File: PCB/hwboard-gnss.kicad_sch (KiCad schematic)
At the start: 1 part, among them U1 TESEO-LIV3R

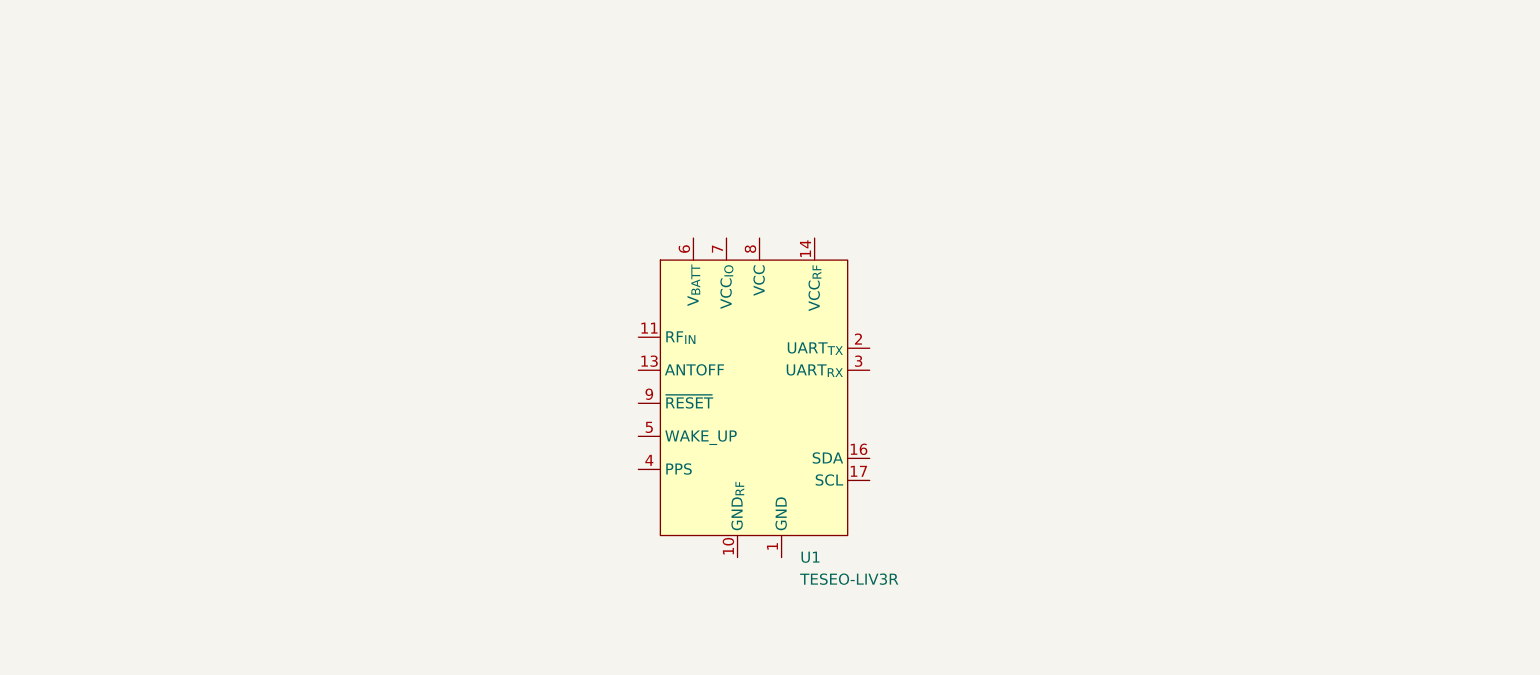
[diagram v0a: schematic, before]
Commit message: Update with gnss
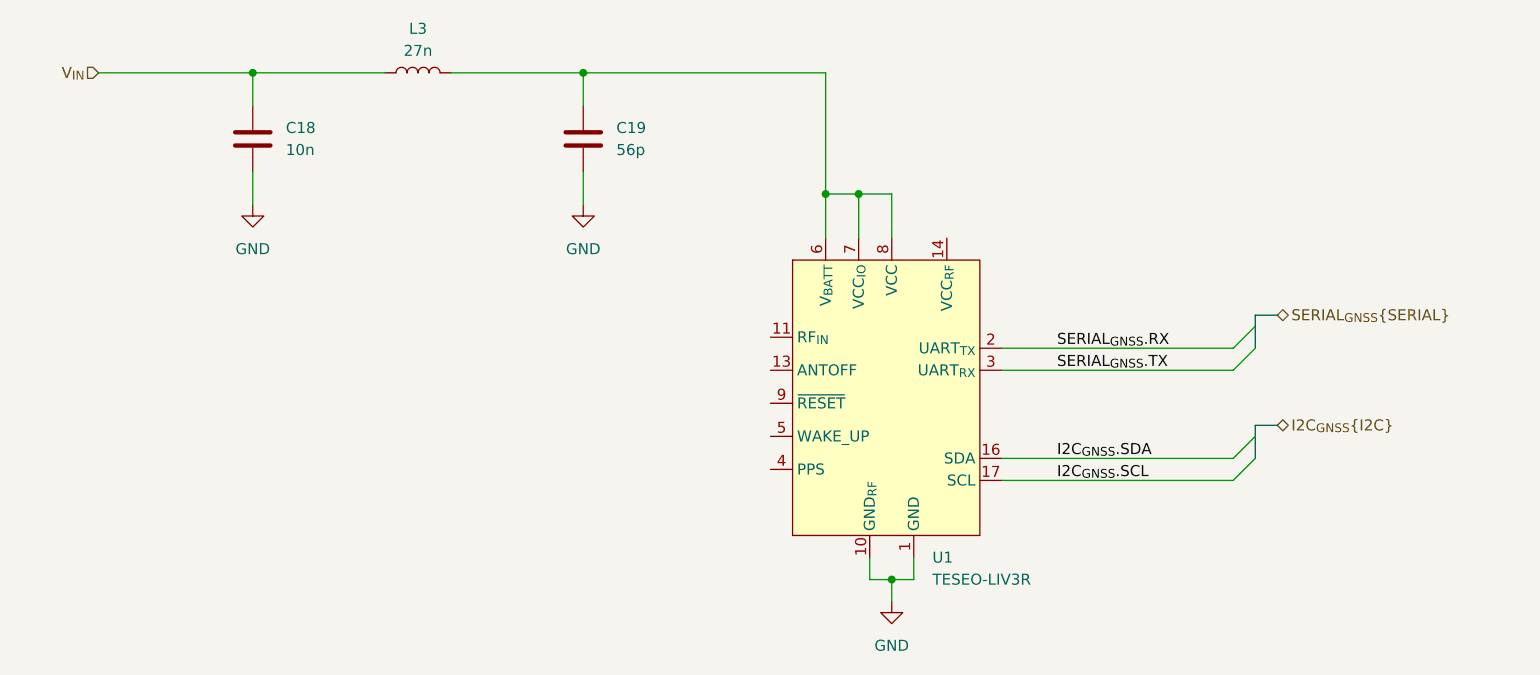
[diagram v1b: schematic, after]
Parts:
- added C18: 10n, symbol Device:C
- added C19: 56p, symbol Device:C
- added L3: 27n, symbol Device:L
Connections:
- net GND_{RF} is gone; now on net GND: U1.10 (GND_{RF}), U1.12 (GND_{RF})
- net GND: now reaches U1.1 (GND)
- net GND: now also C18.2, C19.2
- net I2C_{GNSS}.SDA: now reaches U1.16 (SDA)
- net I2C_{GNSS}.SCL: now reaches U1.17 (SCL)
- net SERIAL_{GNSS}.RX: now reaches U1.2 (UART_{TX})
- net SERIAL_{GNSS}.TX: now reaches U1.3 (UART_{RX})
- net at U1.6 (V_{BATT}): now also U1.7 (VCC_{IO}), U1.8 (VCC), C19.1, L3.2
- new net V_{IN}: C18.1, L3.1
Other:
- moved on the sheet: U1
